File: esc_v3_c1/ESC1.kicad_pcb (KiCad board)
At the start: 2 copper layers, 39 parts, among them J1 Power, J2 Inputs, J3 Output, Q1 IRF4905, Q10 S8050, Q11 S8050, Q12 S8050, Q2 IRF4905, Q3 IRF4905, Q4 S8050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

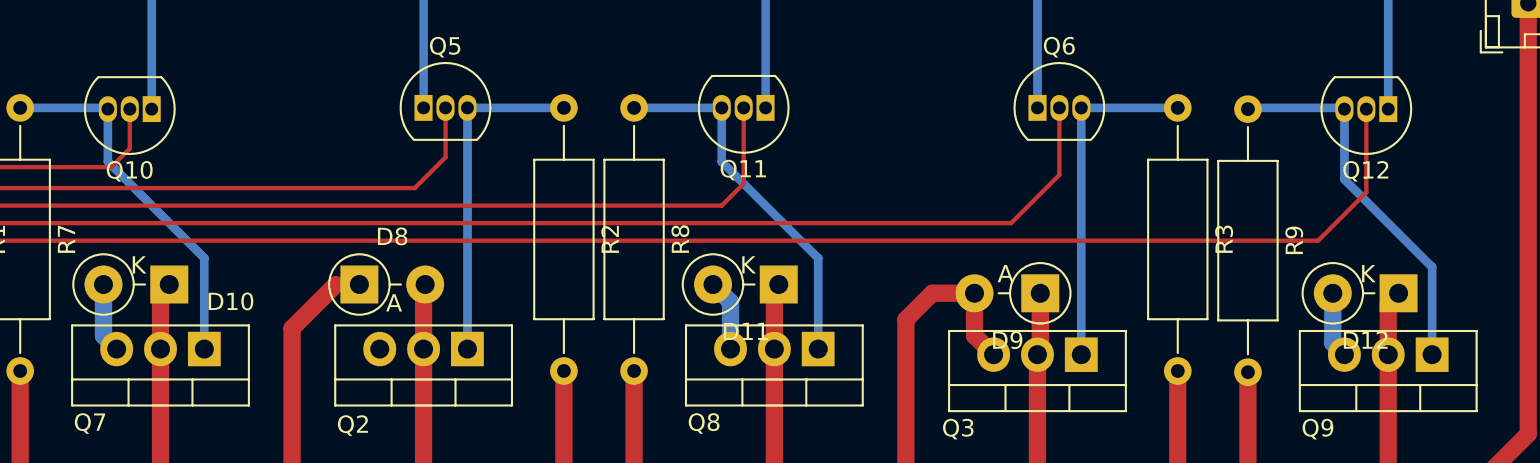
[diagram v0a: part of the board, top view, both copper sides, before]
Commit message: fix n channel driver
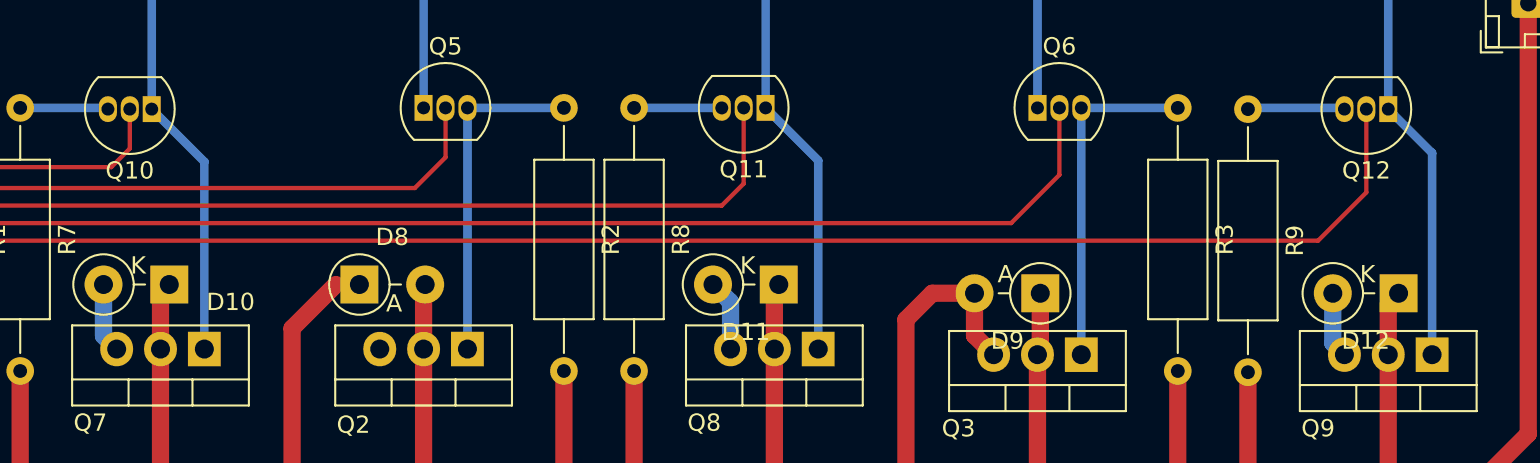
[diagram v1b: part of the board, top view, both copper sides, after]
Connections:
- D5 pad 2: Net-(D5-Pad2) -> Net-(Q8-Pad1)
- Q11 pad 1: Net-(D5-Pad2) -> Net-(Q8-Pad1)
- Q12 pad 3: Net-(Q9-Pad1) -> Net-(Q12-Pad3)
- Q7 pad 1: Net-(Q10-Pad3) -> Net-(D4-Pad2)
- Q8 pad 1: Net-(Q11-Pad3) -> Net-(Q8-Pad1)
- Q9 pad 1: Net-(Q9-Pad1) -> Net-(D6-Pad2)
- R9 pad 1: Net-(Q9-Pad1) -> Net-(Q12-Pad3)
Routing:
- net Net-(Q8-Pad1): track 0.00 -> 27.2 mm
- net Net-(Q9-Pad1): track 21.4 -> 0.00 mm
- net Net-(Q11-Pad3): track 20.9 -> 4.57 mm
- net Net-(Q10-Pad3): track 20.8 -> 4.60 mm
- net Net-(D6-Pad2): track 12.2 -> 27.5 mm
- net Net-(D4-Pad2): track 12.0 -> 27.2 mm
- net Net-(D5-Pad2): track 11.9 -> 0.00 mm
- net Net-(Q12-Pad3): track 0.00 -> 5.11 mm

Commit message: merge.. but the right thing
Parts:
- J1: footprint Connector_JST:JST_XH_B2B-XH-AM_1x02_P2.50mm_Vertical -> Connector_JST:JST_XH_B2B-XH-A_1x02_P2.50mm_Vertical
- moved Q3 21.1 mm to (119.9, 53.9)
- moved Q9 21.1 mm to (140.2, 53.9)
- moved D10 21.1 mm to (67.1, 49.9)
- moved D11 21.1 mm to (102.4, 49.9)
- moved D2 21.1 mm to (81.8, 26.0)
- moved D4 21.1 mm to (64.0, 26.0)
- moved D5 21.1 mm to (99.6, 26.0)
- moved D6 21.1 mm to (135.1, 26.0)
- moved D8 21.1 mm to (78.1, 49.9)
- moved J3 21.1 mm to (145.8, 33.6)
- moved Q11 21.1 mm to (101.6, 39.6)
- moved Q12 21.1 mm to (137.7, 39.7)
- moved Q5 21.1 mm to (81.8, 39.6)
- moved Q7 21.1 mm to (69.1, 53.6)
- moved Q8 21.1 mm to (104.6, 53.6)
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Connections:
- D5 pad 2: Net-(Q8-Pad1) -> Net-(D5-Pad2)
- Q11 pad 1: Net-(Q8-Pad1) -> Net-(D5-Pad2)
- Q7 pad 1: Net-(D4-Pad2) -> Net-(Q10-Pad3)
- Q8 pad 1: Net-(Q8-Pad1) -> Net-(Q11-Pad3)
- Q9 pad 1: Net-(D6-Pad2) -> Net-(Q12-Pad3)
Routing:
- net Net-(Q8-Pad1): track 27.2 -> 0.00 mm
- net Net-(Q12-Pad3): track 5.11 -> 21.4 mm
- net Net-(Q11-Pad3): track 4.57 -> 20.9 mm
- net Net-(Q10-Pad3): track 4.60 -> 20.8 mm
- net Net-(D6-Pad2): track 27.5 -> 12.2 mm
- net Net-(D4-Pad2): track 27.2 -> 12.0 mm
- net Net-(D5-Pad2): track 0.00 -> 11.9 mm
- net VCC: track 261.3 -> 265.5 mm
- net Net-(D12-Pad1): track 84.6 -> 81.6 mm
- net Net-(D10-Pad1): track 184.6 -> 182.4 mm
- net Net-(D11-Pad1): track 136.8 -> 135.0 mm
- net GND: track 13.9 -> 13.0 mm
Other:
- board outline added: 142.2 x 61 mm
- board text added: "A"
- board text added: "A+"
- board text added: "A-"
- board text added: "B"
- board text added: "B+"
- board text added: "B-"
- board text added: "C"
- board text added: "C+"
- board text added: "C-"
- board text added: "ESC Board 3 ©2022 Andrew Woodward-May"
- board text added: "GND"
- board text added: "VCC"
